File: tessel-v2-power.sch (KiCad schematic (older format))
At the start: 60 parts, among them J601 CONN_02X04, J602 CONN_01X03, J603 CONN_01X04, Q601 MMSS8550, U601 AAT4610, U602 AAT4610, U603 AP3417C, U604 AP3417C, U605 AP3418

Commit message: ethernet length-matched
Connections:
- net +3.3V: now also U605.1 (EN)
- net MT_PWR_EN: no longer U605.1 (EN)
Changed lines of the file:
@@
 Text Notes 10900 5300 0    60   ~ 0
 1.8V_SOC
-Text HLabel 10400 5700 0    60   Input ~ 0
-MT_PWR_EN
 $Comp
 L INDUCTOR L603
@@
 Text GLabel 7800 2750 2    60   Input ~ 0
 3.3V_CP
+$Comp
+L +3.3V #PWR0108
+U 1 1 54CB1309
+P 10400 5600
+F 0 "#PWR0108" H 10400 5560 30  0001 C CNN
+F 1 "+3.3V" H 10400 5710 30  0000 C CNN
+F 2 "" H 10400 5600 60  0000 C CNN
+F 3 "" H 10400 5600 60  0000 C CNN
+	1    10400 5600
+	1    0    0    -1
+$EndComp
+Wire Wire Line
+	10400 5700 10400 5600
 $EndSCHEMATC

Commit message: 0603 resistor swapped
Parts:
- C602, C607, C612, C614, C616, C619, C623, C626, C627: footprint tm-kicad-lib:SMD-0402 -> tm-kicad-lib:SMD-0402-C
- C603, C613, C615, C620: footprint SMD_Packages:SMD-0603 -> tm-kicad-lib:SMD-0603-C
- R601, R602, R603, R604, R605, R606, R607, R608, R609, R611, R612, R613, R614, R615, R616, R617: footprint tm-kicad-lib:SMD-0402 -> tm-kicad-lib:SMD-0402-R
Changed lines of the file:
@@
 LIBS:valves
 LIBS:tm-kicad-lib
+LIBS:nordicsemi
 LIBS:tessel-v2-cache
 EELAYER 25 0
@@
 F 0 "R607" V 5630 3100 40  0000 C CNN
 F 1 "450kR 1%" V 5557 3101 40  0000 C CNN
-F 2 "tm-kicad-lib:SMD-0402" V 5480 3100 30  0001 C CNN
+F 2 "tm-kicad-lib:SMD-0402-R" V 5480 3100 30  0001 C CNN
 F 3 "" H 5550 3100 30  0000 C CNN
 	1    5550 3100
@@
 F 0 "C607" H 6700 3300 40  0000 L CNN
 F 1 "100nF" H 6706 3115 40  0000 L CNN
-F 2 "tm-kicad-lib:SMD-0402" H 6738 3050 30  0001 C CNN
+F 2 "tm-kicad-lib:SMD-0402-C" H 6738 3050 30  0001 C CNN
 F 3 "" H 6700 3200 60  0000 C CNN
 	1    6700 3200
@@
 F 0 "R608" V 5630 3800 40  0000 C CNN
 F 1 "100kR 1%" V 5557 3801 40  0000 C CNN
-F 2 "tm-kicad-lib:SMD-0402" V 5480 3800 30  0001 C CNN
+F 2 "tm-kicad-lib:SMD-0402-R" V 5480 3800 30  0001 C CNN
 F 3 "" H 5550 3800 30  0000 C CNN
 	1    5550 3800
@@
 F 0 "C602" H 2450 3350 40  0000 L CNN
 F 1 "10nF" H 2456 3165 40  0000 L CNN
-F 2 "tm-kicad-lib:SMD-0402" H 2488 3100 30  0001 C CNN
+F 2 "tm-kicad-lib:SMD-0402-C" H 2488 3100 30  0001 C CNN
 F 3 "" H 2450 3250 60  0000 C CNN
 	1    2450 3250
@@
 F 0 "C603" H 2850 3350 40  0000 L CNN
 F 1 "4.7uF" H 2856 3165 40  0000 L CNN
-F 2 "SMD_Packages:SMD-0603" H 2888 3100 30  0001 C CNN
+F 2 "tm-kicad-lib:SMD-0603-C" H 2888 3100 30  0001 C CNN
 F 3 "" H 2850 3250 60  0000 C CNN
 	1    2850 3250
@@
 F 0 "R603" V 2780 6150 40  0000 C CNN
 F 1 "33kR" V 2707 6151 40  0000 C CNN
-F 2 "tm-kicad-lib:SMD-0402" V 2630 6150 30  0001 C CNN
+F 2 "tm-kicad-lib:SMD-0402-R" V 2630 6150 30  0001 C CNN
 F 3 "" H 2700 6150 30  0000 C CNN
 	1    2700 6150
@@
 F 0 "C619" H 10900 8900 40  0000 L CNN
 F 1 "100nF" H 10906 8715 40  0000 L CNN
-F 2 "tm-kicad-lib:SMD-0402" H 10938 8650 30  0001 C CNN
+F 2 "tm-kicad-lib:SMD-0402-C" H 10938 8650 30  0001 C CNN
 F 3 "" H 10900 8800 60  0000 C CNN
 	1    10900 8800
@@
 F 0 "C614" H 10200 9600 40  0000 L CNN
 F 1 "100nF" H 10206 9415 40  0000 L CNN
-F 2 "tm-kicad-lib:SMD-0402" H 10238 9350 30  0001 C CNN
+F 2 "tm-kicad-lib:SMD-0402-C" H 10238 9350 30  0001 C CNN
 F 3 "" H 10200 9500 60  0000 C CNN
 	1    10200 9500
@@
 F 0 "C620" H 11300 8900 40  0000 L CNN
 F 1 "4.7uF" H 11306 8715 40  0000 L CNN
-F 2 "SMD_Packages:SMD-0603" H 11338 8650 30  0001 C CNN
+F 2 "tm-kicad-lib:SMD-0603-C" H 11338 8650 30  0001 C CNN
 F 3 "" H 11300 8800 60  0000 C CNN
 	1    11300 8800
@@
 F 0 "R605" V 4580 6450 40  0000 C CNN
 F 1 "1kR" V 4507 6451 40  0000 C CNN
-F 2 "tm-kicad-lib:SMD-0402" V 4430 6450 30  0001 C CNN
+F 2 "tm-kicad-lib:SMD-0402-R" V 4430 6450 30  0001 C CNN
 F 3 "" H 4500 6450 30  0000 C CNN
 	1    4500 6450
@@
 F 0 "R609" V 7680 3600 40  0000 C CNN
 F 1 "1kR" V 7607 3601 40  0000 C CNN
-F 2 "tm-kicad-lib:SMD-0402" V 7530 3600 30  0001 C CNN
+F 2 "tm-kicad-lib:SMD-0402-R" V 7530 3600 30  0001 C CNN
 F 3 "" H 7600 3600 30  0000 C CNN
 	1    7600 3600
@@
 F 0 "R604" V 2780 8750 40  0000 C CNN
 F 1 "33kR" V 2707 8751 40  0000 C CNN
-F 2 "tm-kicad-lib:SMD-0402" V 2630 8750 30  0001 C CNN
+F 2 "tm-kicad-lib:SMD-0402-R" V 2630 8750 30  0001 C CNN
 F 3 "" H 2700 8750 30  0000 C CNN
 	1    2700 8750
@@
 F 0 "R606" V 4580 9050 40  0000 C CNN
 F 1 "1kR" V 4507 9051 40  0000 C CNN
-F 2 "tm-kicad-lib:SMD-0402" V 4430 9050 30  0001 C CNN
+F 2 "tm-kicad-lib:SMD-0402-R" V 4430 9050 30  0001 C CNN
 F 3 "" H 4500 9050 30  0000 C CNN
 	1    4500 9050
@@
 F 0 "R612" V 12730 3100 40  0000 C CNN
 F 1 "450kR 1%" V 12657 3101 40  0000 C CNN
-F 2 "tm-kicad-lib:SMD-0402" V 12580 3100 30  0001 C CNN
+F 2 "tm-kicad-lib:SMD-0402-R" V 12580 3100 30  0001 C CNN
 F 3 "" H 12650 3100 30  0000 C CNN
 	1    12650 3100
@@
 F 0 "C623" H 13800 3300 40  0000 L CNN
 F 1 "100nF" H 13806 3115 40  0000 L CNN
-F 2 "tm-kicad-lib:SMD-0402" H 13838 3050 30  0001 C CNN
+F 2 "tm-kicad-lib:SMD-0402-C" H 13838 3050 30  0001 C CNN
 F 3 "" H 13800 3200 60  0000 C CNN
 	1    13800 3200
@@
 F 0 "R613" V 12730 3800 40  0000 C CNN
 F 1 "100kR 1%" V 12657 3801 40  0000 C CNN
-F 2 "tm-kicad-lib:SMD-0402" V 12580 3800 30  0001 C CNN
+F 2 "tm-kicad-lib:SMD-0402-R" V 12580 3800 30  0001 C CNN
 F 3 "" H 12650 3800 30  0000 C CNN
 	1    12650 3800
@@
 F 0 "C612" H 9550 3350 40  0000 L CNN
 F 1 "10nF" H 9556 3165 40  0000 L CNN
-F 2 "tm-kicad-lib:SMD-0402" H 9588 3100 30  0001 C CNN
+F 2 "tm-kicad-lib:SMD-0402-C" H 9588 3100 30  0001 C CNN
 F 3 "" H 9550 3250 60  0000 C CNN
 	1    9550 3250
@@
 F 0 "C615" H 9950 3350 40  0000 L CNN
 F 1 "4.7uF" H 9956 3165 40  0000 L CNN
-F 2 "SMD_Packages:SMD-0603" H 9988 3100 30  0001 C CNN
+F 2 "tm-kicad-lib:SMD-0603-C" H 9988 3100 30  0001 C CNN
 F 3 "" H 9950 3250 60  0000 C CNN
 	1    9950 3250
@@
 F 0 "R611" V 10330 1500 40  0000 C CNN
 F 1 "10kR" V 10257 1501 40  0000 C CNN
-F 2 "tm-kicad-lib:SMD-0402" V 10180 1500 30  0001 C CNN
+F 2 "tm-kicad-lib:SMD-0402-R" V 10180 1500 30  0001 C CNN
 F 3 "" H 10250 1500 30  0000 C CNN
 	1    10250 1500
@@
 F 0 "R616" V 14780 3600 40  0000 C CNN
 F 1 "1kR" V 14707 3601 40  0000 C CNN
-F 2 "tm-kicad-lib:SMD-0402" V 14630 3600 30  0001 C CNN
+F 2 "tm-kicad-lib:SMD-0402-R" V 14630 3600 30  0001 C CNN
 F 3 "" H 14700 3600 30  0000 C CNN
 	1    14700 3600
@@
 F 0 "R614" V 12730 6050 40  0000 C CNN
 F 1 "200kR 1%" V 12657 6051 40  0000 C CNN
-F 2 "tm-kicad-lib:SMD-0402" V 12580 6050 30  0001 C CNN
+F 2 "tm-kicad-lib:SMD-0402-R" V 12580 6050 30  0001 C CNN
 F 3 "" H 12650 6050 30  0000 C CNN
 	1    12650 6050
@@
 F 0 "C627" H 14600 6250 40  0000 L CNN
 F 1 "100nF" H 14606 6065 40  0000 L CNN
-F 2 "tm-kicad-lib:SMD-0402" H 14638 6000 30  0001 C CNN
+F 2 "tm-kicad-lib:SMD-0402-C" H 14638 6000 30  0001 C CNN
 F 3 "" H 14600 6150 60  0000 C CNN
 	1    14600 6150
@@
 F 0 "R615" V 12730 6750 40  0000 C CNN
 F 1 "100kR 1%" V 12657 6751 40  0000 C CNN
-F 2 "tm-kicad-lib:SMD-0402" V 12580 6750 30  0001 C CNN
+F 2 "tm-kicad-lib:SMD-0402-R" V 12580 6750 30  0001 C CNN
 F 3 "" H 12650 6750 30  0000 C CNN
 	1    12650 6750
@@
 F 0 "C616" H 9950 6300 40  0000 L CNN
 F 1 "10nF" H 9956 6115 40  0000 L CNN
-F 2 "tm-kicad-lib:SMD-0402" H 9988 6050 30  0001 C CNN
+F 2 "tm-kicad-lib:SMD-0402-C" H 9988 6050 30  0001 C CNN
 F 3 "" H 9950 6200 60  0000 C CNN
 	1    9950 6200
@@
 F 0 "C613" H 9550 6300 40  0000 L CNN
 F 1 "4.7uF" H 9556 6115 40  0000 L CNN
-F 2 "SMD_Packages:SMD-0603" H 9588 6050 30  0001 C CNN
+F 2 "tm-kicad-lib:SMD-0603-C" H 9588 6050 30  0001 C CNN
 F 3 "" H 9550 6200 60  0000 C CNN
 	1    9550 6200
@@
 F 0 "R617" V 15580 6550 40  0000 C CNN
 F 1 "330R" V 15507 6551 40  0000 C CNN
-F 2 "tm-kicad-lib:SMD-0402" V 15430 6550 30  0001 C CNN
+F 2 "tm-kicad-lib:SMD-0402-R" V 15430 6550 30  0001 C CNN
 F 3 "" H 15500 6550 30  0000 C CNN
 	1    15500 6550
@@
 F 0 "C626" H 14200 6250 40  0000 L CNN
 F 1 "1uF" H 14206 6065 40  0000 L CNN
-F 2 "tm-kicad-lib:SMD-0402" H 14238 6000 30  0001 C CNN
+F 2 "tm-kicad-lib:SMD-0402-C" H 14238 6000 30  0001 C CNN
 F 3 "" H 14200 6150 60  0000 C CNN
 	1    14200 6150
@@
 F 0 "R601" V 1980 5250 40  0000 C CNN
 F 1 "100kR" V 1907 5251 40  0000 C CNN
-F 2 "tm-kicad-lib:SMD-0402" V 1830 5250 30  0001 C CNN
+F 2 "tm-kicad-lib:SMD-0402-R" V 1830 5250 30  0001 C CNN
 F 3 "" H 1900 5250 30  0000 C CNN
 	1    1900 5250
@@
 F 0 "R602" V 1980 7850 40  0000 C CNN
 F 1 "100kR" V 1907 7851 40  0000 C CNN
-F 2 "tm-kicad-lib:SMD-0402" V 1830 7850 30  0001 C CNN
+F 2 "tm-kicad-lib:SMD-0402-R" V 1830 7850 30  0001 C CNN
 F 3 "" H 1900 7850 30  0000 C CNN
 	1    1900 7850

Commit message: working towards pin muxing for v2v3 and general schematic cleanup
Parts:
- removed J601: CONN_02X04, Pin_Headers:Pin_Header_Straight_2x04, symbol CONN_02X04
- removed J602: CONN_01X03, Pin_Headers:Pin_Header_Straight_1x03, symbol CONN_01X03
- removed J603: CONN_01X04, Pin_Headers:Pin_Header_Straight_1x04, symbol CONN_01X04
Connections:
- net PORTA_PWR_EN renamed PORT_A_PWR_EN
- net PORTB_PWR_EN renamed PORT_B_PWR_EN
- no-connect marks 1 -> 0
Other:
- moved on the sheet: C601, C602, C603, C606, C607, C608, C609, C610, C612, C615, C621, C623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

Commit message: most schematic changes done, major refactoring underway
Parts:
- removed D601, D602, D603, D604, D605: GREEN, LEDs:LED-0603, symbol LED
- removed R605, R606, R609, R616: 1kR, tm-kicad-lib:SMD-0402-R, symbol R
- removed R617: 330R, tm-kicad-lib:SMD-0402-R, symbol R
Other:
- note removed: "3.3V SOC : 33S\n1.8V SOC : 18S\n3.3V COPROCESSOR : 33C\n3.3V PORTS : 33A, 33B\n"
- moved on the sheet: C601, C602, C603, C604, C605, C610, C611, C612, C613, C614, C615, C616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

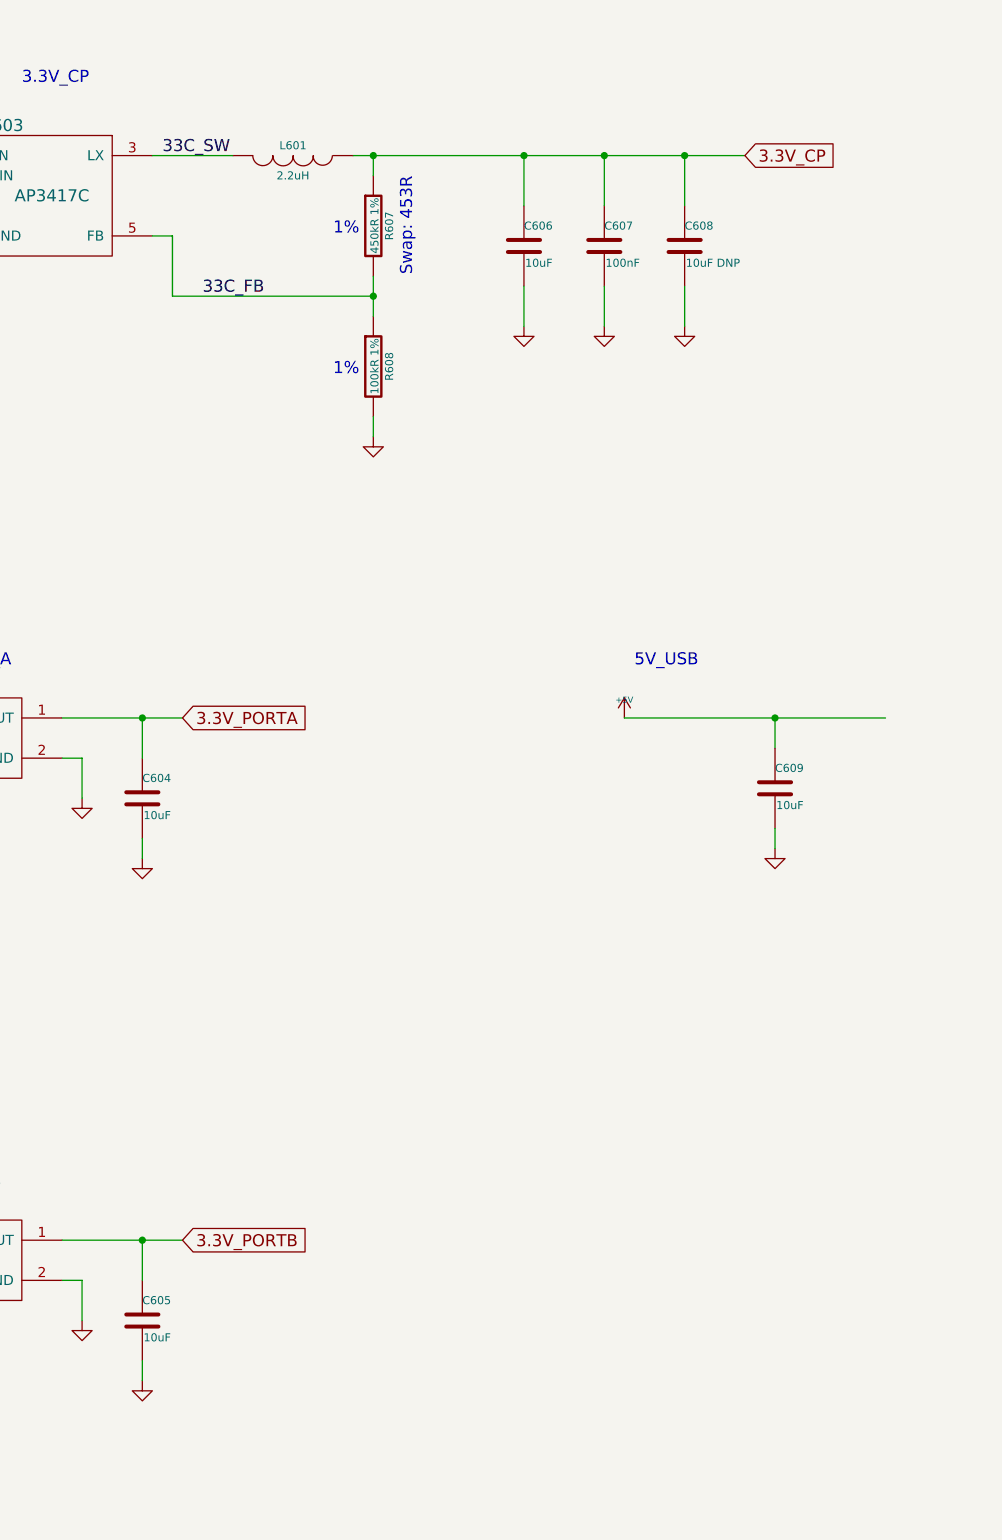
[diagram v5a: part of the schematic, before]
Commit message: last but not least: refactoring mediatek itself
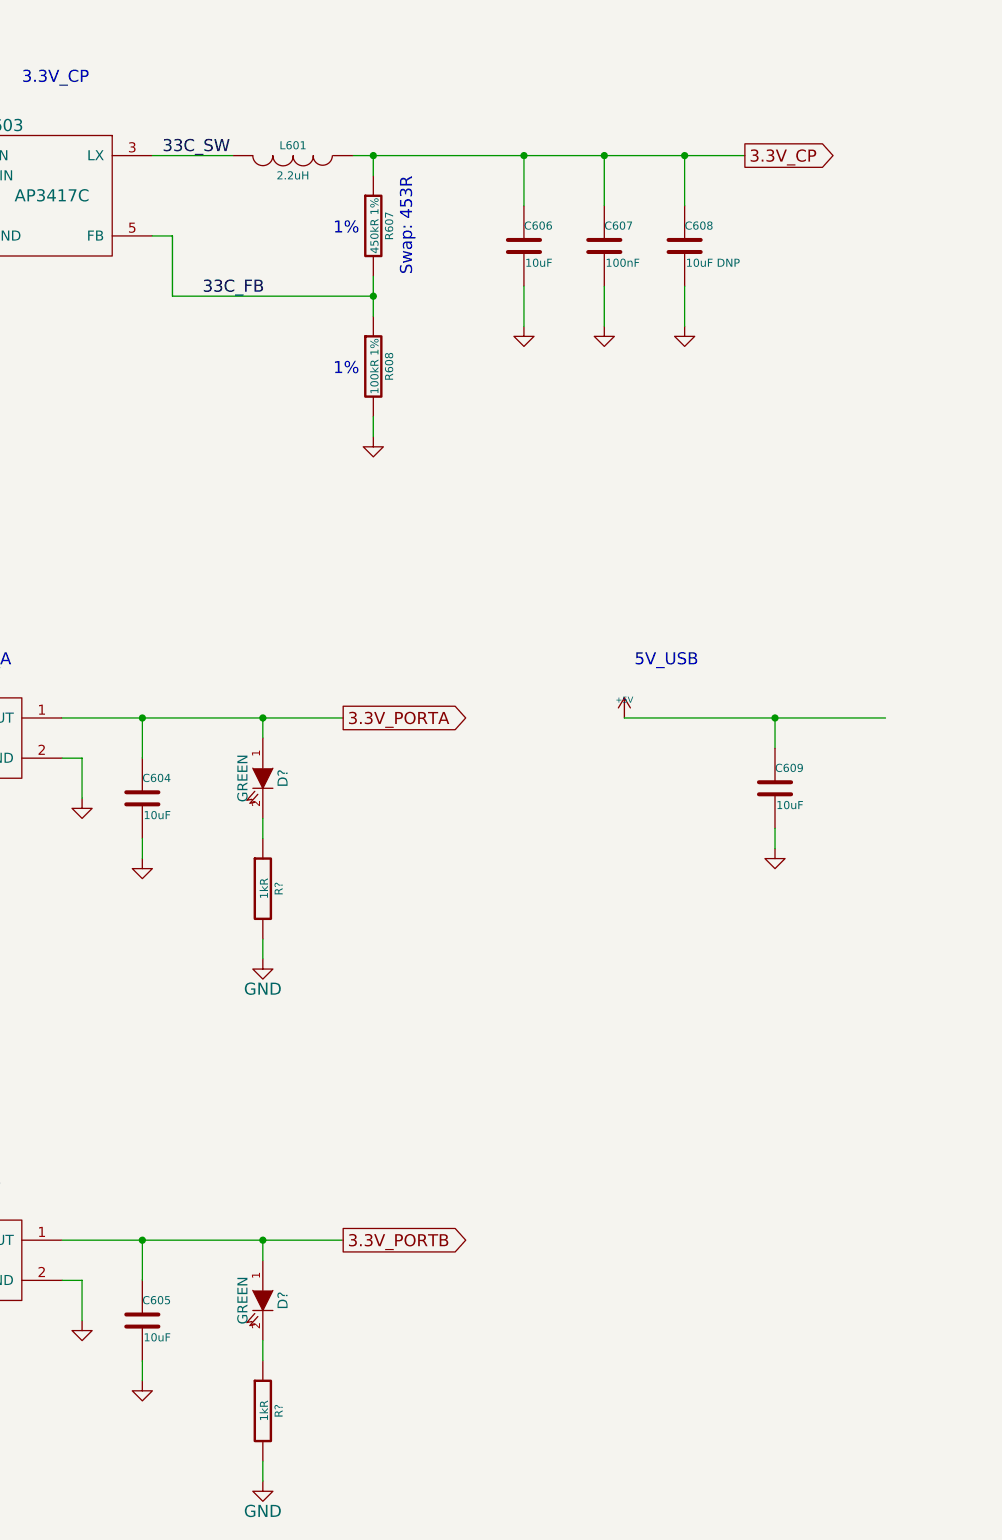
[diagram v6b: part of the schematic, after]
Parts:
- added D? (x2): GREEN, LEDs:LED-0603, symbol LED
- added R? (x2): 1kR, tm-kicad-lib:SMD-0402-R, symbol R
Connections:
- net 3.3V_PORTA: now also D?.1 (A)
- net 3.3V_PORTB: now also D?.1 (A)
- net GND: now also R?.2, R?.2
- new net: D?.2 (K), R?.1 (x2)
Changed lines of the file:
@@
 	1    0    0    -1
 $EndComp
-Text GLabel 4600 5600 2    60   Input ~ 0
+Text GLabel 5400 5600 2    60   Output ~ 0
 3.3V_PORTA
-Text GLabel 4600 8200 2    60   Input ~ 0
+Text GLabel 5400 8200 2    60   Output ~ 0
 3.3V_PORTB
 $Comp
@@
 	1    0    0    -1
 $EndComp
-Text GLabel 7400 2800 2    60   Input ~ 0
+Text GLabel 7400 2800 2    60   Output ~ 0
 3.3V_CP
 $Comp
@@
 	4000 8200 4400 8200
 Wire Wire Line
-	4400 8200 4600 8200
+	4400 8200 5400 8200
 Wire Wire Line
 	1700 8300 1900 8300
@@
 	4000 5600 4400 5600
 Wire Wire Line
-	4400 5600 4600 5600
+	4400 5600 5400 5600
 Wire Wire Line
 	1700 5700 1900 5700
@@
 Text Notes 10300 7700 0    60   ~ 0
 1.2V
+$Comp
+L R R?
+U 1 1 54EC6ACD
+P 5000 6450
+F 0 "R?" V 5080 6450 40  0000 C CNN
+F 1 "1kR" V 5007 6451 40  0000 C CNN
+F 2 "tm-kicad-lib:SMD-0402-R" V 4930 6450 30  0001 C CNN
+F 3 "" H 5000 6450 30  0000 C CNN
+	1    5000 6450
+	1    0    0    -1
+$EndComp
+$Comp
+L LED D?
+U 1 1 54EC6AD4
+P 5000 5900
+F 0 "D?" H 5000 6000 50  0000 C CNN
+F 1 "GREEN" H 5000 5800 50  0000 C CNN
+F 2 "LEDs:LED-0603" H 5000 5900 60  0001 C CNN
+F 3 "" H 5000 5900 60  0000 C CNN
+	1    5000 5900
+	0    1    1    0
+$EndComp
+$Comp
+L GND #PWR?
+U 1 1 54EC6ADB
+P 5000 6800
+F 0 "#PWR?" H 5000 6550 60  0001 C CNN
+F 1 "GND" H 5000 6650 60  0000 C CNN
+F 2 "" H 5000 6800 60  0000 C CNN
+F 3 "" H 5000 6800 60  0000 C CNN
+	1    5000 6800
+	1    0    0    -1
+$EndComp
+Wire Wire Line
+	5000 6100 5000 6200
+Wire Wire Line
+	5000 6700 5000 6800
+Wire Wire Line
+	5000 5600 5000 5700
+Connection ~ 5000 5600
+$Comp
+L R R?
+U 1 1 54EC6BE3
+P 5000 9050
+F 0 "R?" V 5080 9050 40  0000 C CNN
+F 1 "1kR" V 5007 9051 40  0000 C CNN
+F 2 "tm-kicad-lib:SMD-0402-R" V 4930 9050 30  0001 C CNN
+F 3 "" H 5000 9050 30  0000 C CNN
+	1    5000 9050
+	1    0    0    -1
+$EndComp
+$Comp
+L LED D?
+U 1 1 54EC6BE9
+P 5000 8500
+F 0 "D?" H 5000 8600 50  0000 C CNN
+F 1 "GREEN" H 5000 8400 50  0000 C CNN
+F 2 "LEDs:LED-0603" H 5000 8500 60  0001 C CNN
+F 3 "" H 5000 8500 60  0000 C CNN
+	1    5000 8500
+	0    1    1    0
+$EndComp
+$Comp
+L GND #PWR?
+U 1 1 54EC6BEF
+P 5000 9400
+F 0 "#PWR?" H 5000 9150 60  0001 C CNN
+F 1 "GND" H 5000 9250 60  0000 C CNN
+F 2 "" H 5000 9400 60  0000 C CNN
+F 3 "" H 5000 9400 60  0000 C CNN
+	1    5000 9400
+	1    0    0    -1
+$EndComp
+Wire Wire Line
+	5000 8700 5000 8800
+Wire Wire Line
+	5000 9300 5000 9400
+Wire Wire Line
+	5000 8200 5000 8300
+Connection ~ 5000 8200
 $EndSCHEMATC
